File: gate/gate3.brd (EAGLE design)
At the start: 57.1 x 82.5 mm, 32 parts, among them J1 MOLEX_MINILITE_TRAP_2, J2 MOLEX_MINILITE_TRAP_2, J3 MOLEX_MINILITE_TRAP_2, J4 MOLEX_MINILITE_TRAP_2, J8 MOLEX_MINILITE_TRAP_2, J9 MOLEX_MINILITE_TRAP_2, U1 SN75468

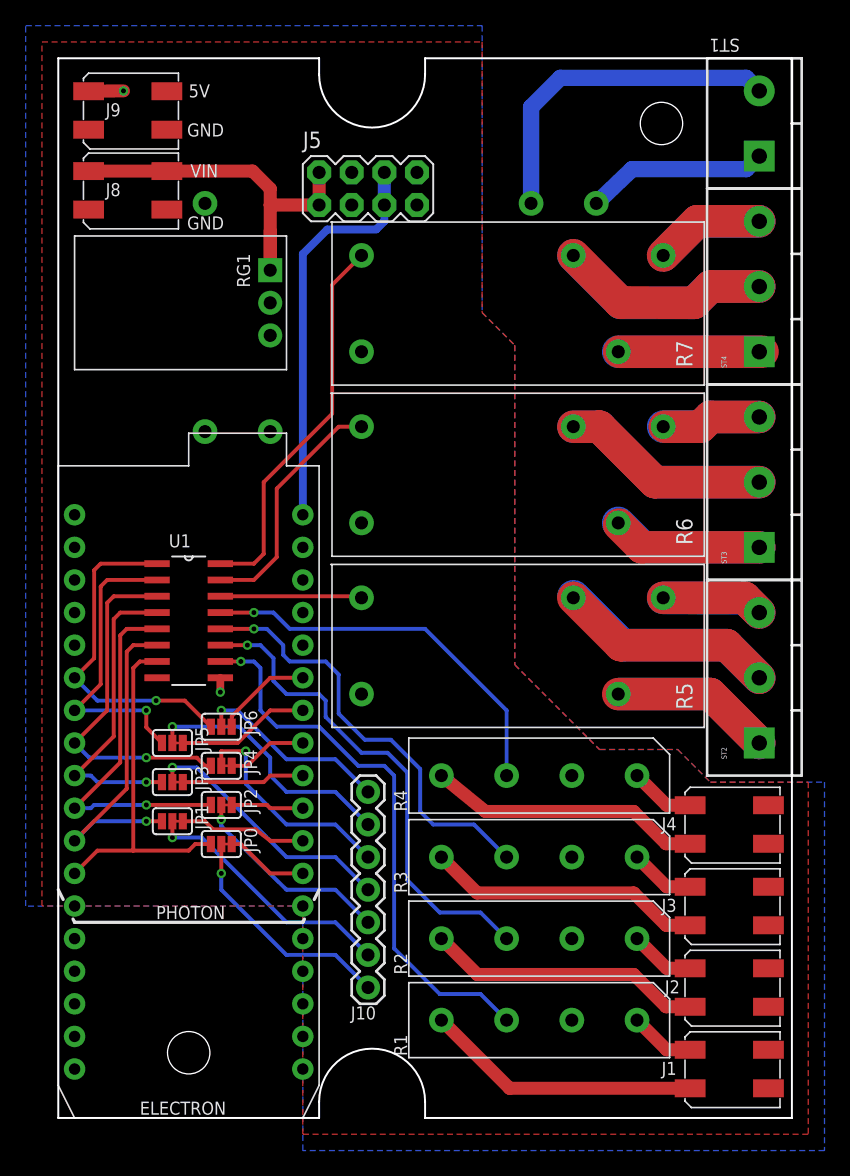
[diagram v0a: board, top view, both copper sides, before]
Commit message: Fix gate3 relay and ps orientation
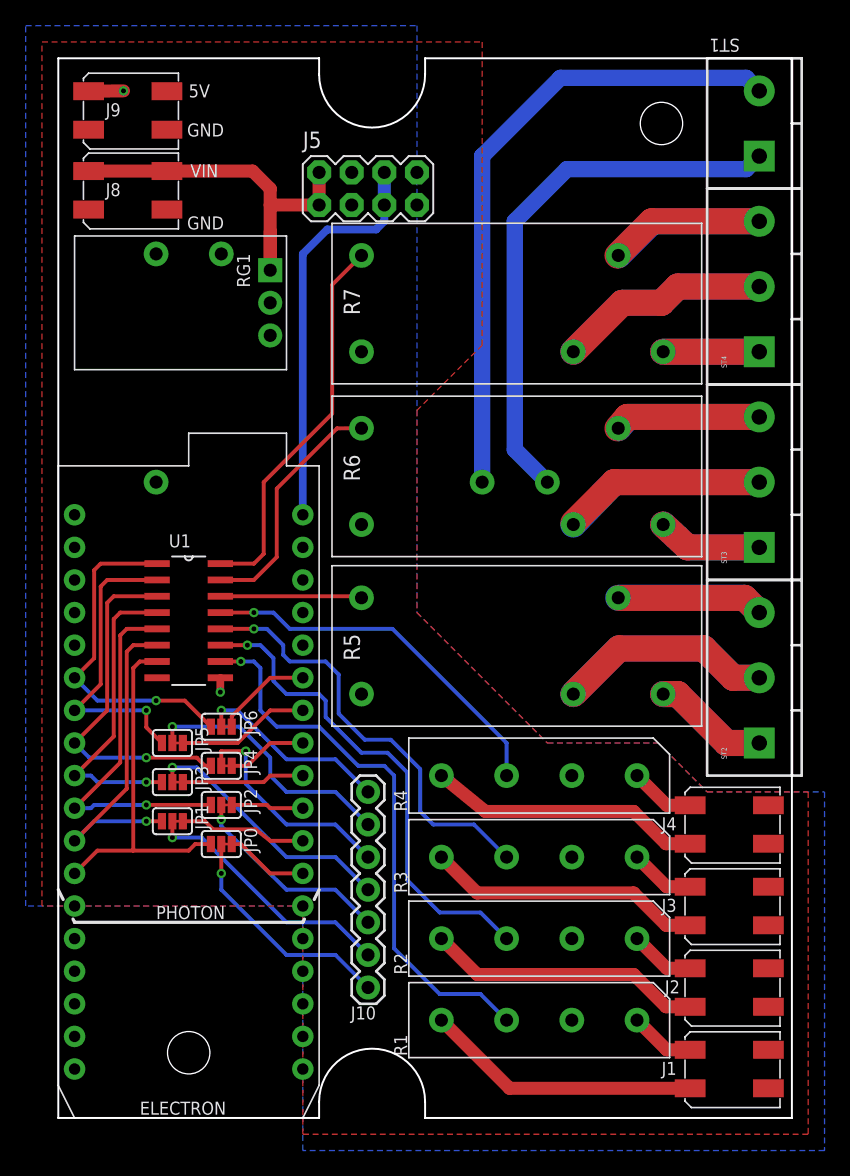
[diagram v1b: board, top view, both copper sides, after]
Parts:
- moved PS1 14.4 mm to (7.62, 67.3), turned to 180 degrees
- moved R6 0.13 mm to (23.6, 46.2)
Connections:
- removed net N$22: R5.NO, ST2.3
- new net N$25: R7.NO, ST4.1
- net N$14: now also R6.NO; no longer R6.C
- net N$16: now also R5.NO; no longer R5.C
- net N$17: now also R5.C, ST2.3; no longer R6.NO, ST3.3
- net N$18: now also R6.C, ST3.3; no longer R7.C, ST4.1
- net N$20: now also R7.C; no longer R7.NO
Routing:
- net N$1: track 14.2 -> 42.5 mm
- net N$23: track 26.6 -> 49.9 mm
- net N$22: track 15.9 -> 0.00 mm
- net N$25: track 0.00 -> 15.0 mm
- net N$18: track 11.0 -> 22.9 mm
- net N$24: track 11.2 -> 0.00 mm
- net N$17: track 15.5 -> 22.9 mm
- net N$20: track 17.2 -> 24.2 mm
- net N$14: track 23.4 -> 16.4 mm
- net N$16: track 25.1 -> 18.1 mm
- net N$2: track 30.5 -> 29.0 mm
- net N$15: track 32.5 -> 31.7 mm
